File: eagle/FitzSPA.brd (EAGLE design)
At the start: 49.2 x 49.5 mm, 32 parts, among them U1 AD9200ARZ, U2 AD8129ARMZ, U3 VAT1-SMT

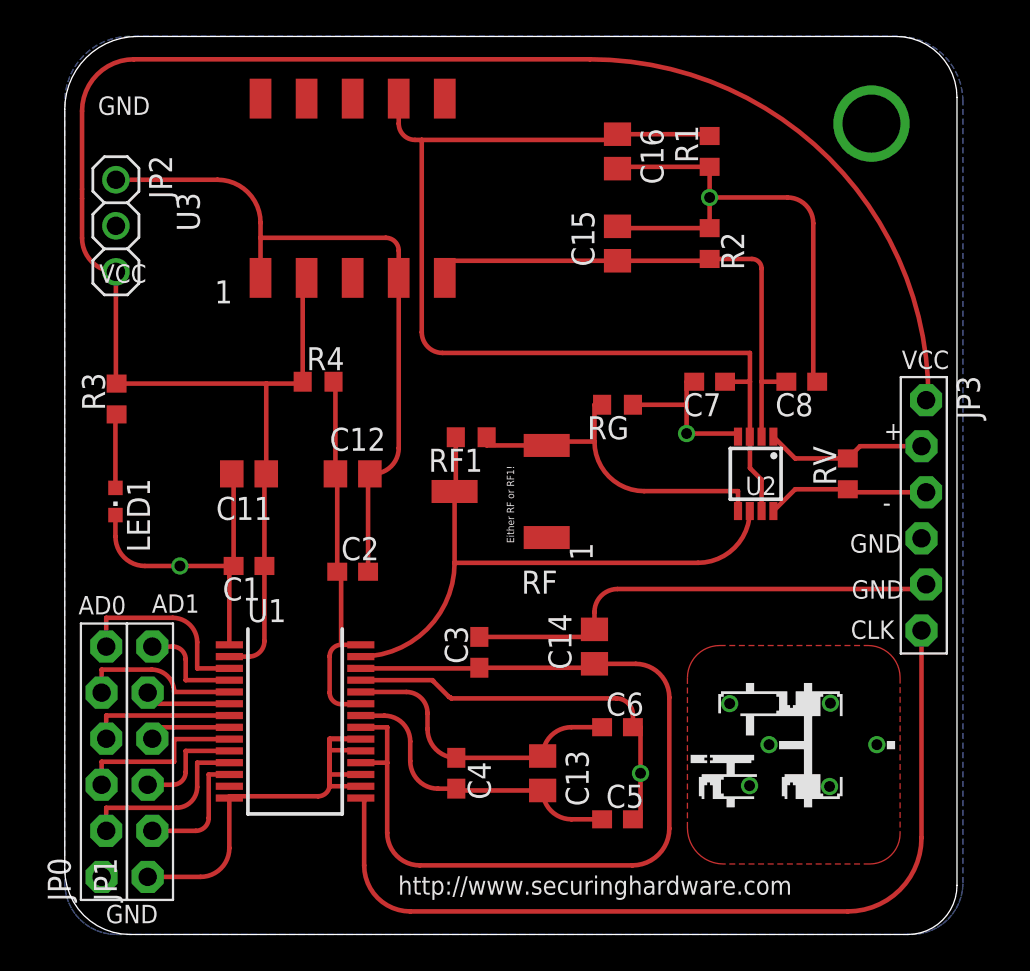
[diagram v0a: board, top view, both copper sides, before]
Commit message: Moving to branches for revisions instead of file names
changed filename
added 2nd POT on pin 4 of the diff amp to give a variable offset
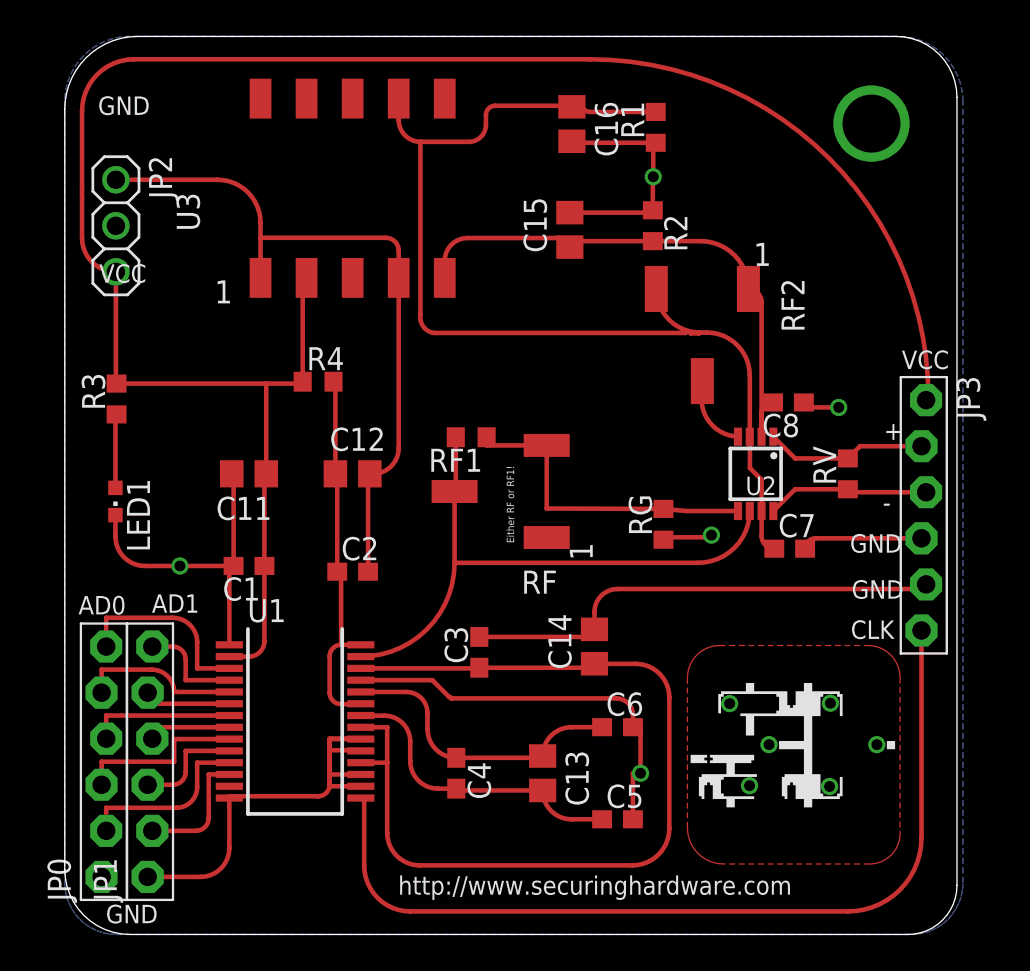
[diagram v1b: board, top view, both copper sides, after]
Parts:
- added RF2: 10kΩ, Model84POT:MODEL84POT
- moved C7 10.2 mm to (40.0, 21.3), turned to 0 degrees
- moved RG 7.06 mm to (33.0, 22.6), turned to 90 degrees
- moved R2 3.28 mm to (32.4, 39.1)
- moved R1 3.25 mm to (32.6, 44.5)
- moved C16 2.93 mm to (28.0, 44.7)
- moved C15 2.74 mm to (27.9, 38.9)
- moved C8 1.36 mm to (39.9, 29.3)
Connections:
- new net N$23: RF2.P$2, U2.4
- net +12V: now also RF2.P$3
- net -12V: now also RF2.P$1
- net GND: no longer U2.4
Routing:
- net GND: track 171.3 -> 158.6 mm, vias 10 -> 11
- net N$23: track 0.00 -> 4.01 mm
- net -12V: track 29.4 -> 30.9 mm
- net +12V: track 58.9 -> 60.0 mm
- net N$3: track 19.1 -> 18.1 mm
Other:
- board text added: "FitzSPA 1.1"
- board text removed: "FitzSPA 1.0"
